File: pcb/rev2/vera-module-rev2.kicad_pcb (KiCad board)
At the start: 2 copper layers, 96.5 x 55 mm, 119 parts, among them J1 Bus, J2 Prog, J3 SD_Card, J4 Composite, J5 VGA, J6 Conn_01x04, J7 Conn_01x02, J8 RS232, J9 S-video, U1 ICE40UP5K-SG48ITR50, U10 MIC5504-3.3YM5, U11 THS7314D, U12 MAX3221CPWR, U2 74AHC00PW, U3 SN74CBTD3861PWR, U4 74AHC1G14GW,125, U5 74LVC4245APW, U6 WM8524CGEDT, U7 W25Q16JVSNIQ, U8 74AHC1G14GW,125, U9 AP3417CKTR-G1, X1 SG5032CAN_25.000000M-TJGA3

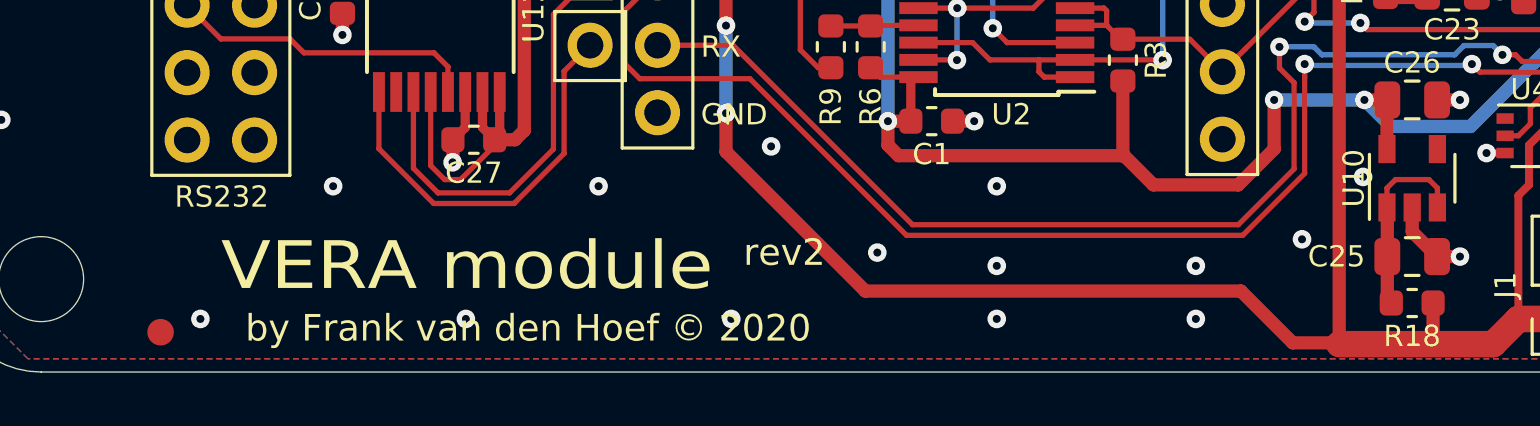
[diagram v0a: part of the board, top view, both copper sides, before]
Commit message: Rev2 PCB: added X16 logo.
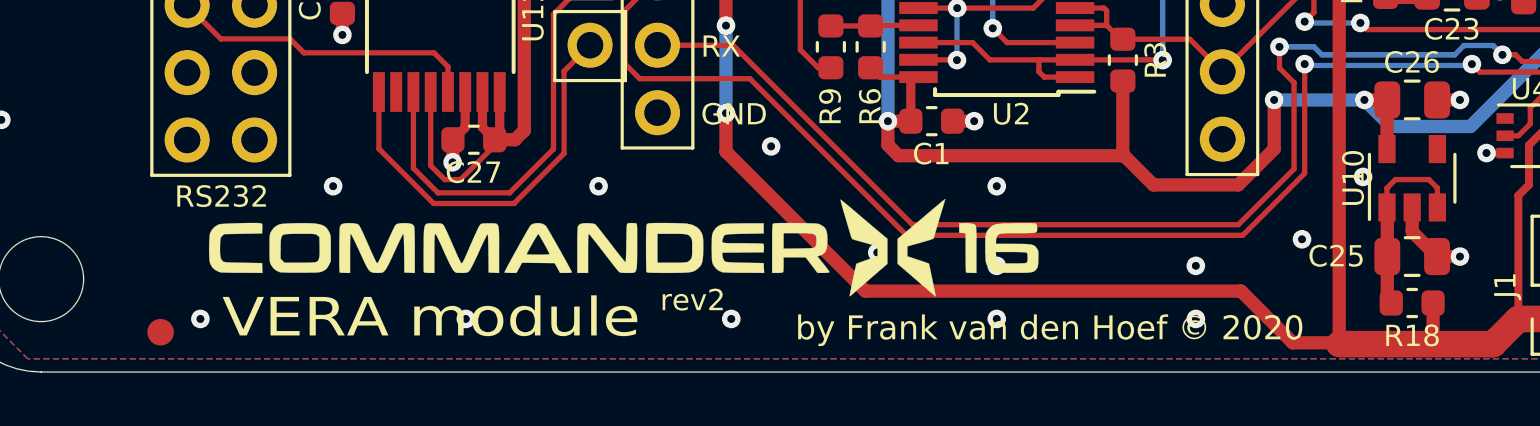
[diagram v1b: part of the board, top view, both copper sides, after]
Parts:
- added LOGO1: X16 logo, vera-module:x16logo, F.Cu at (127.0, 130.3)
